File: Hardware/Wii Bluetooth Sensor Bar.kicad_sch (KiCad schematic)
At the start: 16 parts, among them J1 USB_C_Receptacle_USB2.0, J2 USB_A, SW1 SW_Push, U1 J27H002, U2 LM1117-3.3

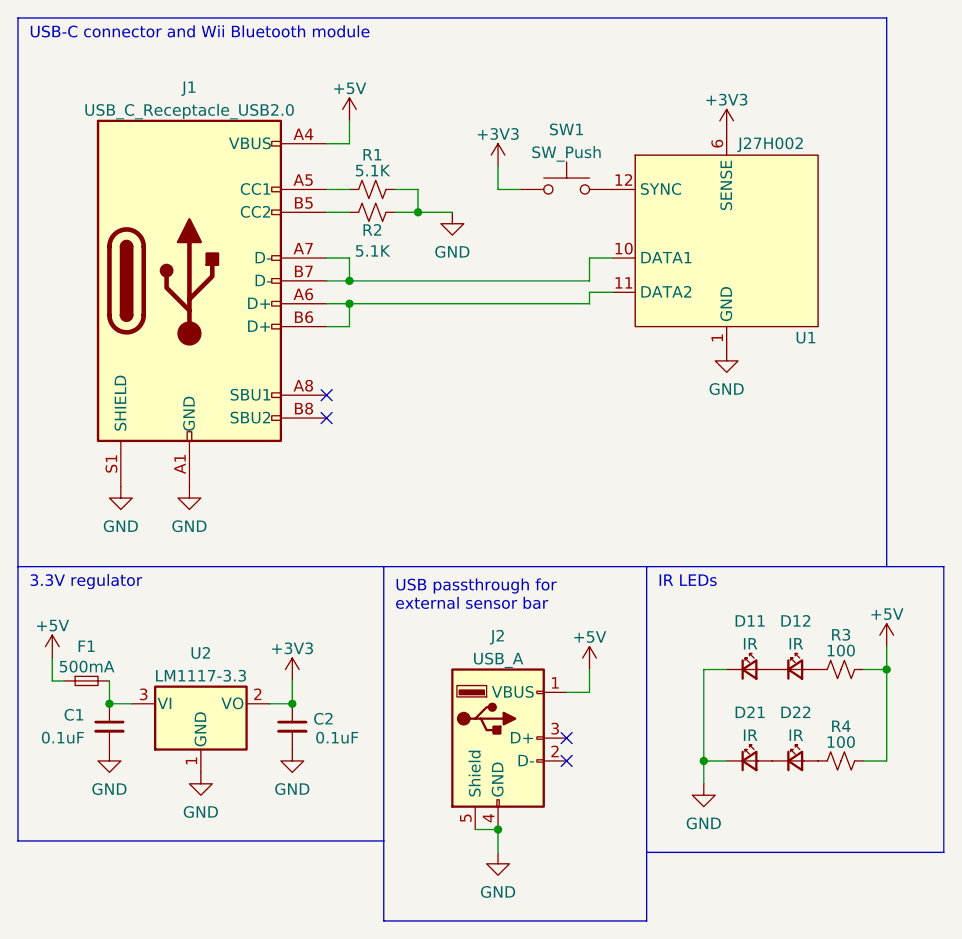
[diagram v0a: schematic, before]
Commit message: Finish footprint assignment and rough PCB layout
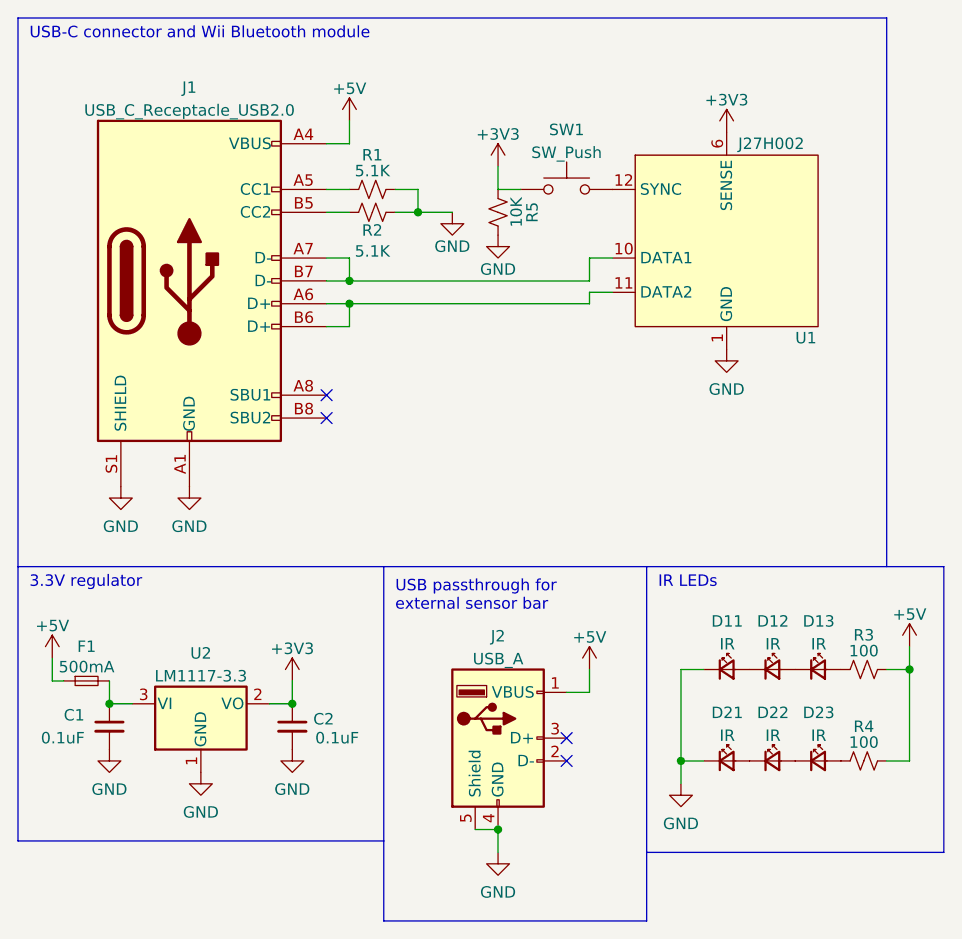
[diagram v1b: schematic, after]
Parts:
- added D13, D23: IR, LED_SMD:LED_1206_3216Metric_Pad1.42x1.75mm_HandSolder, symbol Device:LED_Small
- added R5: 10K, Resistor_SMD:R_0805_2012Metric_Pad1.20x1.40mm_HandSolder, symbol Device:R_Small_US
- C1, C2: footprint Capacitor_SMD:C_0603_1608Metric_Pad1.08x0.95mm_HandSolder -> Capacitor_SMD:C_0805_2012Metric_Pad1.18x1.45mm_HandSolder
- F1: footprint Fuse:Fuse_0603_1608Metric_Pad1.05x0.95mm_HandSolder -> Fuse:Fuse_0805_2012Metric_Pad1.15x1.40mm_HandSolder
- J1: footprint (none) -> Connector_USB_Other:USB_C_Receptacle_Amphenol_C12402012
- J2: footprint (none) -> Connector_USB:USB_A_Molex_67643_Horizontal
- R1, R2, R3, R4: footprint Resistor_SMD:R_0603_1608Metric_Pad0.98x0.95mm_HandSolder -> Resistor_SMD:R_0805_2012Metric_Pad1.20x1.40mm_HandSolder
- U1: footprint (none) -> Connector_Other:J27H002
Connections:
- net +3V3: now also R5.1
- net GND: now also R5.2
- net at D12.2 (A): now also D13.1 (K); no longer R3.1
- net at D22.2 (A): now also D23.1 (K); no longer R4.1
- new net: D23.2 (A), R4.1
- new net: D13.2 (A), R3.1
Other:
- moved on the sheet: D11, D12, D21, D22, R3, R4

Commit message: Finish Rev A PCB
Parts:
- removed D11, D12, D13, D21, D22, D23: IR, LED_SMD:LED_1206_3216Metric_Pad1.42x1.75mm_HandSolder, symbol Device:LED_Small
- removed R3, R4: 100, Resistor_SMD:R_0805_2012Metric_Pad1.20x1.40mm_HandSolder, symbol Device:R_Small_US
- added J1: LED_Left, Connector_PinHeader_2.54mm:PinHeader_1x02_P2.54mm_Vertical, symbol Connector:Conn_01x02_Male
- added J2: LED_Right, Connector_PinHeader_2.54mm:PinHeader_1x02_P2.54mm_Vertical, symbol Connector:Conn_01x02_Male
- renumbered J1 to USB1, J2 to USB2
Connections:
- net +5V: now also J1.1 (Pin_1), J2.1 (Pin_1)
- net GND: now also J1.2 (Pin_2), J2.2 (Pin_2)

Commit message: Fix incorrect sync button footprint
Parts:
- SW1: footprint Button_Switch_SMD:SW_SPST_EVPBF -> Button_Switch_SMD:SW_SPST_PTS645
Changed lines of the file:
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@@
     (property "Reference" "SW1" (id 0) (at 149.86 60.6892 0))
     (property "Value" "SW_Push" (id 1) (at 149.86 63.2261 0))
-    (property "Footprint" "Button_Switch_SMD:SW_SPST_EVPBF" (id 2) (at 149.86 62.23 0)
+    (property "Footprint" "Button_Switch_SMD:SW_SPST_PTS645" (id 2) (at 149.86 62.23 0)
       (effects (font (size 1.27 1.27)) hide)
     )
@@
     )
     (path "/cb65760f-2d83-45ce-9a0c-0348210c8df1"
-      (reference "SW1") (unit 1) (value "SW_Push") (footprint "Button_Switch_SMD:SW_SPST_EVPBF")
+      (reference "SW1") (unit 1) (value "SW_Push") (footprint "Button_Switch_SMD:SW_SPST_PTS645")
     )
     (path "/f80c0469-32e9-4925-a676-945ba1955c35"

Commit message: Fix #2
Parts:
- R1, R2: PN (none) -> CRG0805F5K1
- R5: PN (none) -> RNCP0805FTD10K0
- SW1: PN (none) -> PTS645SL43SMTR92 LFS
- U1: PN (none) -> J27H002
- USB1: PN (none) -> 12402012E212A
- USB2: PN (none) -> USB-A1HSW6
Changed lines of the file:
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@@
       (effects (font (size 1.27 1.27)) hide)
     )
-    (property "Datasheet" "~" (id 3) (at 142.24 69.85 0)
+    (property "Datasheet" "https://www.seielect.com/catalog/sei-rncp.pdf" (id 3) (at 142.24 69.85 0)
+      (effects (font (size 1.27 1.27)) hide)
+    )
+    (property "PN" "RNCP0805FTD10K0" (id 4) (at 142.24 69.85 90)
       (effects (font (size 1.27 1.27)) hide)
     )
@@
     )
     (property "Datasheet" "https://www.usb.org/sites/default/files/documents/usb_type-c.zip" (id 3) (at 111.76 77.47 0)
+      (effects (font (size 1.27 1.27)) hide)
+    )
+    (property "PN" "12402012E212A" (id 4) (at 107.95 77.47 0)
       (effects (font (size 1.27 1.27)) hide)
     )
@@
       (effects (font (size 1.27 1.27)) hide)
     )
-    (property "Datasheet" "~" (id 3) (at 128.27 67.31 0)
+    (property "Datasheet" "https://www.te.com/commerce/DocumentDelivery/DDEController?Action=srchrtrv&DocNm=1773204&DocType=DS&DocLang=English" (id 3) (at 128.27 67.31 0)
+      (effects (font (size 1.27 1.27)) hide)
+    )
+    (property "PN" "CRG0805F5K1" (id 4) (at 128.27 67.31 90)
       (effects (font (size 1.27 1.27)) hide)
     )
@@
       (effects (font (size 1.27 1.27)) hide)
     )
-    (property "Datasheet" "~" (id 3) (at 149.86 62.23 0)
+    (property "Datasheet" "https://www.ckswitches.com/media/1471/pts645.pdf" (id 3) (at 149.86 62.23 0)
+      (effects (font (size 1.27 1.27)) hide)
+    )
+    (property "PN" "PTS645SL43SMTR92 LFS" (id 4) (at 149.86 67.31 0)
       (effects (font (size 1.27 1.27)) hide)
     )
@@
       (effects (font (size 1.27 1.27)) hide)
     )
-    (property "Datasheet" " ~" (id 3) (at 146.05 129.54 0)
+    (property "Datasheet" "http://www.on-shore.com/wp-content/uploads/USB-A1HSXX.pdf" (id 3) (at 146.05 129.54 0)
+      (effects (font (size 1.27 1.27)) hide)
+    )
+    (property "PN" "USB-A1HSW6" (id 4) (at 142.24 128.27 0)
       (effects (font (size 1.27 1.27)) hide)
     )
@@
       (effects (font (size 1.27 1.27)) hide)
     )
-    (property "Datasheet" "" (id 3) (at 156.21 58.42 0)
+    (property "Datasheet" "https://fccid.io/MCLJ27H002/User-Manual/Users-Manual-721663.pdf" (id 3) (at 156.21 58.42 0)
+      (effects (font (size 1.27 1.27)) hide)
+    )
+    (property "PN" "J27H002" (id 4) (at 167.64 73.66 0)
       (effects (font (size 1.27 1.27)) hide)
     )
@@
       (effects (font (size 1.27 1.27)) hide)
     )
-    (property "Datasheet" "~" (id 3) (at 128.27 69.85 0)
-      (effects (font (size 1.27 1.27)) hide)
-    )
+    (property "Datasheet" "https://www.te.com/commerce/DocumentDelivery/DDEController?Action=srchrtrv&DocNm=1773204&DocType=DS&DocLang=English" (id 3) (at 128.27 69.85 0)
+      (effects (font (size 1.27 1.27)) hide)
+    )
+    (property "PN" "CRG0805F5K1" (id 4) (at 128.27 69.85 90)
+      (effects (font (size 1.27 1.27)) hide)
+    )

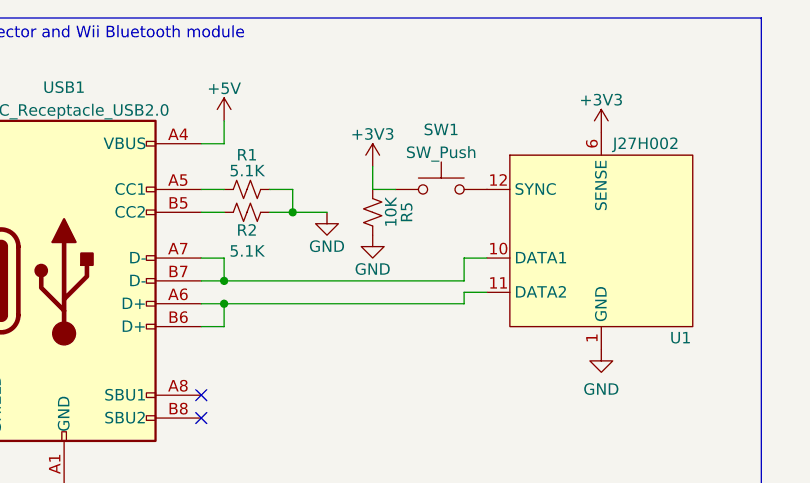
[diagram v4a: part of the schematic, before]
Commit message: Fix bad pulldown resistor
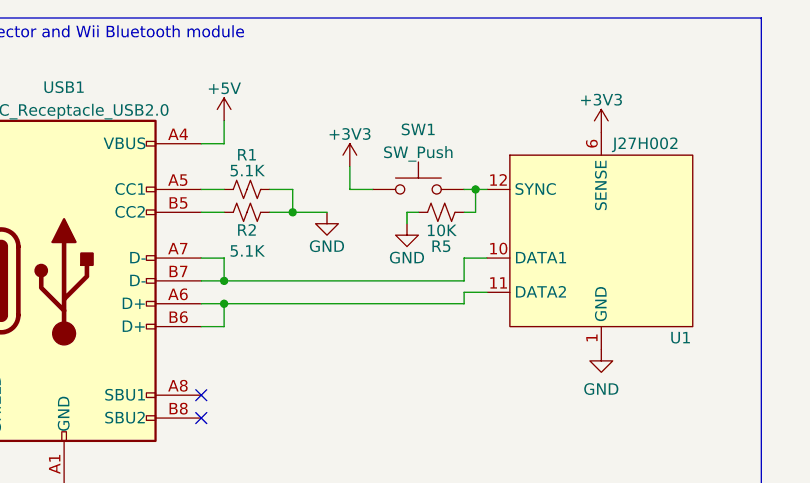
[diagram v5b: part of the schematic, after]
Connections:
- net +3V3: no longer R5.1
- net at SW1.2, U1.12 (SYNC): now also R5.1
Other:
- moved on the sheet: R5, SW1
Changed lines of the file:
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@@
   (junction (at 184.15 119.38) (diameter 0) (color 0 0 0 0)
+  )
+  (junction (at 153.67 67.31) (diameter 0) (color 0 0 0 0)
   )
   (junction (at 99.06 124.46) (diameter 0) (color 0 0 0 0)
@@
   (no_connect (at 149.86 128.27))
   (no_connect (at 149.86 130.81))
+  (wire (pts (xy 139.7 64.77) (xy 139.7 67.31))
+    (stroke (width 0) (type default) (color 0 0 0 0))
+  )
   (wire (pts (xy 123.19 69.85) (xy 125.73 69.85))
     (stroke (width 0) (type default) (color 0 0 0 0))
@@
     (stroke (width 0) (type default) (color 0 0 0 0))
   )
-  (wire (pts (xy 142.24 64.77) (xy 142.24 67.31))
-    (stroke (width 0) (type default) (color 0 0 0 0))
-  )
-  (wire (pts (xy 142.24 67.31) (xy 144.78 67.31))
+  (wire (pts (xy 146.05 69.85) (xy 146.05 71.12))
     (stroke (width 0) (type default) (color 0 0 0 0))
   )
@@
     (stroke (width 0) (type default) (color 0 0 0 0))
   )
+  (wire (pts (xy 153.67 69.85) (xy 152.4 69.85))
+    (stroke (width 0) (type default) (color 0 0 0 0))
+  )
   (wire (pts (xy 125.73 59.69) (xy 125.73 62.23))
     (stroke (width 0) (type default) (color 0 0 0 0))
@@
     (stroke (width 0) (type default) (color 0 0 0 0))
   )
+  (wire (pts (xy 153.67 67.31) (xy 154.94 67.31))
+    (stroke (width 0) (type default) (color 0 0 0 0))
+  )
   (wire (pts (xy 152.4 78.74) (xy 152.4 80.01))
     (stroke (width 0) (type default) (color 0 0 0 0))
   )
+  (wire (pts (xy 152.4 67.31) (xy 153.67 67.31))
+    (stroke (width 0) (type default) (color 0 0 0 0))
+  )
   (wire (pts (xy 123.19 74.93) (xy 125.73 74.93))
     (stroke (width 0) (type default) (color 0 0 0 0))
@@
     (stroke (width 0) (type default) (color 0 0 0 0))
   )
+  (wire (pts (xy 139.7 67.31) (xy 142.24 67.31))
+    (stroke (width 0) (type default) (color 0 0 0 0))
+  )
   (wire (pts (xy 125.73 82.55) (xy 125.73 80.01))
     (stroke (width 0) (type default) (color 0 0 0 0))
@@
     (stroke (width 0) (type default) (color 0 0 0 0))
   )
+  (wire (pts (xy 147.32 69.85) (xy 146.05 69.85))
+    (stroke (width 0) (type default) (color 0 0 0 0))
+  )
   (wire (pts (xy 123.19 77.47) (xy 125.73 77.47))
     (stroke (width 0) (type default) (color 0 0 0 0))
@@
   )
   (wire (pts (xy 119.38 124.46) (xy 116.84 124.46))
+    (stroke (width 0) (type default) (color 0 0 0 0))
+  )
+  (wire (pts (xy 153.67 67.31) (xy 153.67 69.85))
     (stroke (width 0) (type default) (color 0 0 0 0))
   )
@@
     (pin "1")
   )
-  (symbol (lib_id "power:+3V3") (at 142.24 64.77 0) (unit 1)
-    (in_bom yes) (on_board yes) (fields_autoplaced)
-    (property "Reference" "#PWR0112" (id 0) (at 142.24 68.58 0)
-      (effects (font (size 1.27 1.27)) hide)
-    )
-    (property "Value" "+3V3" (id 1) (at 142.24 61.1942 0))
-    (property "Footprint" "" (id 2) (at 142.24 64.77 0)
-      (effects (font (size 1.27 1.27)) hide)
-    )
-    (property "Datasheet" "" (id 3) (at 142.24 64.77 0)
+  (symbol (lib_id "power:+3V3") (at 139.7 64.77 0) (unit 1)
+    (in_bom yes) (on_board yes) (fields_autoplaced)
+    (property "Reference" "#PWR0112" (id 0) (at 139.7 68.58 0)
+      (effects (font (size 1.27 1.27)) hide)
+    )
+    (property "Value" "+3V3" (id 1) (at 139.7 61.1942 0))
+    (property "Footprint" "" (id 2) (at 139.7 64.77 0)
+      (effects (font (size 1.27 1.27)) hide)
+    )
+    (property "Datasheet" "" (id 3) (at 139.7 64.77 0)
       (effects (font (size 1.27 1.27)) hide)
     )
@@
     (pin "1")
   )
-  (symbol (lib_id "Device:R_Small_US") (at 142.24 69.85 0) (unit 1)
-    (in_bom yes) (on_board yes)
-    (property "Reference" "R5" (id 0) (at 146.05 69.85 90))
-    (property "Value" "10K" (id 1) (at 144.2919 69.85 90))
-    (property "Footprint" "Resistor_SMD:R_0805_2012Metric_Pad1.20x1.40mm_HandSolder" (id 2) (at 142.24 69.85 0)
-      (effects (font (size 1.27 1.27)) hide)
-    )
-    (property "Datasheet" "https://www.seielect.com/catalog/sei-rncp.pdf" (id 3) (at 142.24 69.85 0)
-      (effects (font (size 1.27 1.27)) hide)
-    )
-    (property "PN" "RNCP0805FTD10K0" (id 4) (at 142.24 69.85 90)
+  (symbol (lib_id "Device:R_Small_US") (at 149.86 69.85 270) (unit 1)
+    (in_bom yes) (on_board yes)
+    (property "Reference" "R5" (id 0) (at 149.86 73.66 90))
+    (property "Value" "10K" (id 1) (at 149.86 71.9019 90))
+    (property "Footprint" "Resistor_SMD:R_0805_2012Metric_Pad1.20x1.40mm_HandSolder" (id 2) (at 149.86 69.85 0)
+      (effects (font (size 1.27 1.27)) hide)
+    )
+    (property "Datasheet" "https://www.seielect.com/catalog/sei-rncp.pdf" (id 3) (at 149.86 69.85 0)
+      (effects (font (size 1.27 1.27)) hide)
+    )
+    (property "PN" "RNCP0805FTD10K0" (id 4) (at 149.86 69.85 90)
       (effects (font (size 1.27 1.27)) hide)
     )
@@
     (pin "2")
   )
-  (symbol (lib_id "power:GND") (at 142.24 72.39 0) (unit 1)
-    (in_bom yes) (on_board yes)
-    (property "Reference" "#PWR0117" (id 0) (at 142.24 78.74 0)
-      (effects (font (size 1.27 1.27)) hide)
-    )
-    (property "Value" "GND" (id 1) (at 142.24 76.2 0))
-    (property "Footprint" "" (id 2) (at 142.24 72.39 0)
-      (effects (font (size 1.27 1.27)) hide)
-    )
-    (property "Datasheet" "" (id 3) (at 142.24 72.39 0)
+  (symbol (lib_id "power:GND") (at 146.05 71.12 0) (unit 1)
+    (in_bom yes) (on_board yes)
+    (property "Reference" "#PWR0117" (id 0) (at 146.05 77.47 0)
+      (effects (font (size 1.27 1.27)) hide)
+    )
+    (property "Value" "GND" (id 1) (at 146.05 74.93 0))
+    (property "Footprint" "" (id 2) (at 146.05 71.12 0)
+      (effects (font (size 1.27 1.27)) hide)
+    )
+    (property "Datasheet" "" (id 3) (at 146.05 71.12 0)
       (effects (font (size 1.27 1.27)) hide)
     )
@@
     (pin "1")
   )
-  (symbol (lib_id "Switch:SW_Push") (at 149.86 67.31 0) (unit 1)
-    (in_bom yes) (on_board yes) (fields_autoplaced)
-    (property "Reference" "SW1" (id 0) (at 149.86 60.6892 0))
-    (property "Value" "SW_Push" (id 1) (at 149.86 63.2261 0))
-    (property "Footprint" "Button_Switch_SMD:SW_SPST_PTS645" (id 2) (at 149.86 62.23 0)
-      (effects (font (size 1.27 1.27)) hide)
-    )
-    (property "Datasheet" "https://www.ckswitches.com/media/1471/pts645.pdf" (id 3) (at 149.86 62.23 0)
-      (effects (font (size 1.27 1.27)) hide)
-    )
-    (property "PN" "PTS645SL43SMTR92 LFS" (id 4) (at 149.86 67.31 0)
-      (effects (font (size 1.27 1.27)) hide)
-    )
+  (symbol (lib_id "Switch:SW_Push") (at 147.32 67.31 0) (unit 1)
+    (in_bom yes) (on_board yes) (fields_autoplaced)
+    (property "Reference" "SW1" (id 0) (at 147.32 60.6892 0))
+    (property "Value" "SW_Push" (id 1) (at 147.32 63.2261 0))
+    (property "Footprint" "Button_Switch_SMD:SW_SPST_PTS645" (id 2) (at 147.32 62.23 0)
+      (effects (font (size 1.27 1.27)) hide)
+    )
+    (property "Datasheet" "https://www.ckswitches.com/media/1471/pts645.pdf" (id 3) (at 147.32 62.23 0)
+      (effects (font (size 1.27 1.27)) hide)
+    )
+    (property "PN" "PTS645SL43SMTR92 LFS" (id 4) (at 147.32 67.31 0)
+      (effects (font (size 1.27 1.27)) hide)
+    )
